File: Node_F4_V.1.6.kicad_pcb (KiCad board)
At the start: 2 copper layers, 56 x 100 mm, 171 parts, among them IC2 MP1584EN, J1 Conn_Jack-DC, J2 Conn_02x12_Odd_Even, J3 Micro_SD_Card, J4 RF_IPEX_U.FL-R-SMT, J5 Conn_01x06, J6 Conn_01x06, J7 RS485, J8 LoRa_Anten, Q2 MMBT3904L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

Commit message: DI track
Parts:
- removed C50: 5.6pF, Anh_Footprints:C_0603
- removed C54: 100nF, Anh_Footprints:C_0603
- removed C58: 10uF, Anh_Footprints:C_0603
- removed C59: 1uF, Anh_Footprints:C_0603
- removed R46: TBD, Anh_Footprints:R_0603
- removed Z2: D_Zener, IVS_FOOTPRINTS:D_MiniMELF
- added C39: NC, Anh_Footprints:C_0603, F.Cu at (124.5, 54.8)
- added C41: 100nF, Anh_Footprints:C_0603, F.Cu at (138.3, 85.4)
- added R23: 10K, Anh_Footprints:R_0603, F.Cu at (155.7, 78.2)
- C51: value 2.4pF -> NC
- C71, C72: value 6.8pF -> NC
- D9, Q2, Q3: footprint IVS_FOOTPRINTS:SOT23-3 -> Anh_Footprints:SOT23-3
- J2: value Conn_02x12_Odd_Even -> IDC_LCD_KEYPAD
- J4: footprint Connector_Coaxial:U.FL_Hirose_U.FL-R-SMT-1_Vertical -> Anh_Footprints:IPEX_Antena_Connector
- J5: value Conn_01x06 -> SWD
- J6: value Conn_01x06 -> WiFi_Prog
- L4: value 2.7nH -> 2.2nH
- U4: footprint Package_SO:SOIC-8_5.23x5.23mm_P1.27mm -> Anh_Footprints:SOIC-8_5.23x5.23
- U5: footprint IVS_FOOTPRINTS:SOIC-16W_7.5x10.3mm_P1.27mm -> Package_SO:SOIC-16W_7.5x10.3mm_P1.27mm
- Y1, Y2: footprint IVS_FOOTPRINTS:Crystal_SMD_5032-4Pin_5.0x3.2mm -> Anh_Footprints:Crystal_3225_4P_1-4
- moved Q2 85.4 mm to (155.2, 80.6)
- moved C9 79.5 mm to (140.2, 116.2), turned to 90 degrees
- moved C51 78.5 mm to (124.5, 50.5), turned to 180 degrees
- moved C55 76.9 mm to (120.2, 51.8), turned to 180 degrees
- moved C52 76.6 mm to (122.3, 54.1), turned to -90 degrees
- moved L5 76.6 mm to (121.0, 54.1), turned to -90 degrees
- moved C38 76.3 mm to (128.9, 53.8), turned to 0 degrees
- moved L4 75.6 mm to (125.2, 52.6)
- moved BZ1 75.4 mm to (146.2, 86.2), turned to 90 degrees
- moved C10 74.8 mm to (126.8, 54.5), turned to 90 degrees
- moved C40 74.4 mm to (128.9, 55.3), turned to 180 degrees
- moved R42 73.9 mm to (156.5, 84.2), turned to -90 degrees
- moved C56 73.8 mm to (119.5, 54.1)
- moved D11 73.8 mm to (151.4, 106.1), turned to 180 degrees
- moved C53 73.3 mm to (119.6, 60.8)
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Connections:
- C45 pad 2: Net-(C45-Pad2) -> Net-(U6-XTAL_P)
- J7 pad 1: GND -> /A+
- J7 pad 2: /A+ -> /B-
- J7 pad 3: /B- -> GND
- L4 pad 1: Net-(U6-LNA_IN) -> Net-(J4-In)
- L4 pad 2: GND -> Net-(U6-LNA_IN)
- U3 pad 1: /BUZZER -> unconnected-(U3-PE2-Pad1)
- U3 pad 7: unconnected-(U3-PC13-Pad7) -> Net-(D1-A)
- U3 pad 71: unconnected-(U3-PA12-Pad71) -> /BUZZER
- U3 pad 72: unconnected-(U3-PA13-Pad72) -> /SWDIO
- U3 pad 76: unconnected-(U3-PA14-Pad76) -> /SWCLK
- U3 pad 9: Net-(D1-A) -> unconnected-(U3-PC15-Pad9)
- Y2 pad 1: Net-(C45-Pad2) -> Net-(U6-XTAL_P)
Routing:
- net +3.3V: track 107.0 -> 404.6 mm, vias 0 -> 28
- net GND: track 7.19 -> 59.0 mm, vias 0 -> 6
- net /SWDIO: track 0.00 -> 48.6 mm, vias 0 -> 1
- net VCC: track 0.00 -> 46.3 mm, vias 0 -> 2
- net /ESP_RX: track 1.55 -> 45.2 mm
- net /I2C_SCL: track 0.00 -> 41.0 mm, vias 0 -> 2
- net /SWCLK: track 0.00 -> 40.0 mm, vias 0 -> 1
- net /I2C_SDA: track 0.00 -> 38.4 mm, vias 0 -> 2
- net /UART_TX_LOG: track 0.00 -> 34.7 mm, vias 0 -> 1
- net /UART_RX_LOG: track 0.00 -> 33.9 mm, vias 0 -> 1
- net /ESP_TX: track 10.8 -> 43.3 mm
- net /LORA NSS: track 0.00 -> 30.7 mm, vias 0 -> 2
- net /SPI_MOSI: track 0.00 -> 28.6 mm, vias 0 -> 2
- net /RS485_RO: track 1.48 -> 28.5 mm, vias 0 -> 2
- net /SPI_MISO: track 0.00 -> 26.6 mm, vias 0 -> 2
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- added copper zone on B.Cu, net GND
- added copper zone on F.Cu, net GND

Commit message: 50%
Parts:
- removed C41: 100nF, Anh_Footprints:C_0603
- removed D1: LED_Blink, Anh_Footprints:LED_0603
- removed R13: 470, Anh_Footprints:R_0603
- removed R36, R37, R38, R39, R40: 10k, Anh_Footprints:R_0603
- added C50: 1u, Anh_Footprints:C_0603, F.Cu at (100.1, 118.2)
- added C54: 100n, Anh_Footprints:C_0603, F.Cu at (98.4, 118.2)
- added D12: LED, Anh_Footprints:LED_0603, F.Cu at (116.4, 75.2)
- added D13: LED, Anh_Footprints:LED_0603, F.Cu at (120.1, 75.2)
- added D2: LED, Anh_Footprints:LED_0603, F.Cu at (108.8, 75.3)
- added D6: LED, Anh_Footprints:LED_0603, F.Cu at (112.6, 75.2)
- added Q1: P_Mosfet, Anh_Footprints:SOT23-3, F.Cu at (82.5, 101.8)
- added R24: 1M, Anh_Footprints:R_0603, F.Cu at (85.2, 101.6)
- added R25: 220, Anh_Footprints:R_0603, F.Cu at (108.8, 76.7)
- added R26: 220, Anh_Footprints:R_0603, F.Cu at (112.6, 76.6)
- added R27: 220, Anh_Footprints:R_0603, F.Cu at (116.4, 76.6)
- added R28: 220, Anh_Footprints:R_0603, F.Cu at (120.1, 76.6)
- added U7: W25Q128JVS, IVS_FOOTPRINTS:SOIC-8_5.23x5.23mm_P1.27mm, F.Cu at (92.8, 120.1)
- C13: footprint Anh_Footprints:C_0603 -> Anh_Footprints:C_1210
- J2: value IDC_LCD_KEYPAD -> Conn_01x10; footprint Connector_IDC:IDC-Header_2x12_P2.54mm_Vertical -> IVS_FOOTPRINTS:XH 2.54 10Pin Female
- J3: value Micro_SD_Card -> Conn_01x16_Female; footprint Anh_Footprints:MicroSD_Socket_9P -> Connector_PinSocket_2.54mm:PinSocket_1x16_P2.54mm_Vertical
- moved H1 124.2 mm to (75.7, 122.4), turned to 180 degrees
- moved H4 115.3 mm to (75.7, 69.3), turned to 180 degrees
- moved H2 93.5 mm to (167.7, 122.4), turned to 180 degrees
- moved C26 88.5 mm to (86.3, 114.7), turned to 180 degrees
- moved C6 87.6 mm to (86.3, 113.0), turned to 180 degrees
- moved C25 83.2 mm to (86.9, 101.6), turned to 90 degrees
- moved H3 81.2 mm to (167.7, 69.3), turned to 180 degrees
- moved L1 78.5 mm to (88.4, 95.3), turned to 0 degrees
- moved C19 78.1 mm to (88.4, 97.0), turned to 0 degrees
- moved C12 77.7 mm to (88.4, 98.7), turned to 180 degrees
- moved C28 73.8 mm to (92.3, 97.1), turned to 90 degrees
- moved C24 69.4 mm to (94.0, 97.2), turned to 90 degrees
- moved C8 68.4 mm to (94.9, 94.7), turned to 180 degrees
- moved Y1 66.6 mm to (96.5, 91.9), turned to 180 degrees
- moved R3 64.9 mm to (96.4, 97.0), turned to 0 degrees
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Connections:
- J2 pad 1: GND -> unconnected-(J2-Pin_1-Pad1)
- J2 pad 2: unconnected-(J2-Pin_2-Pad2) -> /C1
- J2 pad 3: +3.3V -> /C2
- J2 pad 4: unconnected-(J2-Pin_4-Pad4) -> /C3
- J2 pad 5: /TFT_CS -> /C4
- J2 pad 6: unconnected-(J2-Pin_6-Pad6) -> /H1
- J2 pad 7: /TFT_RS -> /H2
- J2 pad 8: unconnected-(J2-Pin_8-Pad8) -> /H3
- J2 pad 9: /TFT_WR -> /H4
- J3 pad 1: /SD_D2 -> GND
- J3 pad 2: /SD_D3 -> +3.3V
- J3 pad 3: /SD_CMD -> /TFT_CS
- J3 pad 4: +3.3V -> /TFT_RS
- J3 pad 5: /SD_CLK -> /TFT_WR
- J3 pad 6: GND -> /TFT_RD
- J3 pad 7: /SD_D0 -> /TFT_RST
- J3 pad 8: /SD_D1 -> Net-(J3-Pin_8)
- J3 pad 9: GND -> /TFT_DB0
- U3 pad 1: unconnected-(U3-PE2-Pad1) -> /TFT_RST
- U3 pad 2: unconnected-(U3-PE3-Pad2) -> /TFT_RD
- U3 pad 3: unconnected-(U3-PE4-Pad3) -> /TFT_WR
- U3 pad 39: unconnected-(U3-PE8-Pad39) -> /TFT_DB0
- U3 pad 4: unconnected-(U3-PE5-Pad4) -> /TFT_RS
- U3 pad 40: unconnected-(U3-PE9-Pad40) -> /TFT_DB1
- U3 pad 41: unconnected-(U3-PE10-Pad41) -> /TFT_DB2
- U3 pad 42: unconnected-(U3-PE11-Pad42) -> /TFT_DB3
- U3 pad 43: unconnected-(U3-PE12-Pad43) -> /TFT_DB4
- U3 pad 44: unconnected-(U3-PE13-Pad44) -> /TFT_DB5
- U3 pad 45: unconnected-(U3-PE14-Pad45) -> /TFT_DB6
- U3 pad 46: unconnected-(U3-PE15-Pad46) -> /TFT_DB7
- U3 pad 48: unconnected-(U3-PB11-Pad48) -> /BUZZER
- U3 pad 5: unconnected-(U3-PE6-Pad5) -> /TFT_CS
- U3 pad 51: unconnected-(U3-PB12-Pad51) -> /W25Q_CS
- U3 pad 65: /SD_D0 -> unconnected-(U3-PC8-Pad65)
- U3 pad 66: /SD_D1 -> unconnected-(U3-PC9-Pad66)
- U3 pad 7: Net-(D1-A) -> unconnected-(U3-PC13-Pad7)
- U3 pad 71: /BUZZER -> unconnected-(U3-PA12-Pad71)
- U3 pad 77: unconnected-(U3-PA15-Pad77) -> /H1
- U3 pad 78: /SD_D2 -> /H2
- U3 pad 79: /SD_D3 -> /H3
- U3 pad 80: /SD_CLK -> /H4
- U3 pad 81: unconnected-(U3-PD0-Pad81) -> /C4
- U3 pad 82: unconnected-(U3-PD1-Pad82) -> /C3
- U3 pad 83: /SD_CMD -> /C2
- U3 pad 84: unconnected-(U3-PD3-Pad84) -> /C1
- U3 pad 98: unconnected-(U3-PE1-Pad98) -> /TFT_LED
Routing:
- net /BUZZER: track 2.09 -> 97.8 mm, vias 0 -> 2
- net +3.3V: track 404.6 -> 497.1 mm, vias 28 -> 13
- net /H4: track 0.00 -> 80.4 mm, vias 0 -> 1
- net /C1: track 0.00 -> 78.4 mm, vias 0 -> 1
- net /H3: track 0.00 -> 76.7 mm, vias 0 -> 1
- net /C2: track 0.00 -> 75.7 mm, vias 0 -> 1
- net /C3: track 0.00 -> 72.8 mm, vias 0 -> 1
- net /H2: track 0.00 -> 70.9 mm, vias 0 -> 1
- net /C4: track 0.00 -> 70.8 mm, vias 0 -> 1
- net /SPI_MOSI: track 28.6 -> 96.7 mm
- net /H1: track 0.00 -> 67.5 mm, vias 0 -> 1
- net /SPI_SCK: track 24.3 -> 89.4 mm, vias 2 -> 3
- net /SPI_MISO: track 26.6 -> 91.2 mm
- net /LORA_RST: track 20.3 -> 80.0 mm, vias 0 -> 2
- net GND: track 59.0 -> 0.00 mm, vias 6 -> 66
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- added copper zone on F.Cu, net Net-(D8-K)
- added copper zone on F.Cu, net Net-(F1-Pad1)
- added copper zone on F.Cu, net Net-(JP2-A)
- added copper zone on F.Cu, net VCC
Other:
- board size 56 x 100 mm -> 97.5 x 59 mm
- board text added: "3v3"
- board text added: "BOOT"
- board text added: "CLK"
- board text added: "DIO"
- board text added: "ESP NAP CODE"
- board text added: "GND"
- board text added: "RST"
- board text added: "RX"
- board text added: "STM NAP CODE"
- board text added: "TX"

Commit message: Xep linh kien
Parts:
- moved BT1 42.0 mm to (87.8, 97.6), turned to 90 degrees
- moved SW1 31.9 mm to (91.6, 118.3), turned to -90 degrees
- moved J6 31.2 mm to (99.2, 118.2)
- moved SW3 31.1 mm to (86.8, 118.3), turned to 90 degrees
- moved C12 29.0 mm to (114.4, 85.8)
- moved C19 28.9 mm to (114.4, 84.4)
- moved L1 28.8 mm to (114.4, 83.0)
- moved U7 28.6 mm to (118.9, 108.4), turned to 180 degrees
- moved C42 27.1 mm to (89.0, 113.8)
- moved C3 26.8 mm to (86.2, 113.8)
- moved SW2 26.6 mm to (82.5, 118.3), turned to -90 degrees
- moved R11 26.6 mm to (87.6, 113.8)
- moved R24 25.9 mm to (108.2, 89.8)
- moved C8 25.8 mm to (117.8, 82.8)
- moved C24 25.8 mm to (116.8, 85.1)
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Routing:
- net +3.3V: track 497.1 -> 14.7 mm, vias 13 -> 0
- net /BUZZER: track 97.8 -> 0.00 mm, vias 2 -> 0
- net /SPI_MOSI: track 96.7 -> 0.00 mm, vias 2 -> 0
- net /SPI_MISO: track 91.2 -> 0.00 mm, vias 2 -> 0
- net /SPI_SCK: track 89.4 -> 0.00 mm, vias 3 -> 0
- net /LORA NSS: track 86.8 -> 0.00 mm, vias 2 -> 0
- net /H4: track 80.4 -> 0.00 mm, vias 1 -> 0
- net /LORA_RST: track 80.0 -> 0.00 mm, vias 2 -> 0
- net /LORA_DIO1: track 78.9 -> 0.00 mm, vias 2 -> 0
- net /C1: track 78.4 -> 0.00 mm, vias 1 -> 0
- net /LORA_DIO0: track 78.4 -> 0.00 mm, vias 2 -> 0
- net /H3: track 76.7 -> 0.00 mm, vias 1 -> 0
- net /C2: track 75.7 -> 0.00 mm, vias 1 -> 0
- net /C3: track 72.8 -> 0.00 mm, vias 1 -> 0
- net /H2: track 70.9 -> 0.00 mm, vias 1 -> 0
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- removed copper zone on B.Cu, net GND
- removed copper zone on F.Cu, net GND
- removed copper zone on F.Cu, net Net-(D8-K)
- removed copper zone on F.Cu, net Net-(F1-Pad1)
- removed copper zone on F.Cu, net Net-(JP2-A)
- removed copper zone on F.Cu, net VCC
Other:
- board text removed: "3v3"
- board text removed: "BOOT"
- board text removed: "CLK"
- board text removed: "DIO"
- board text removed: "ESP NAP CODE"
- board text removed: "GND"
- board text removed: "RST"
- board text removed: "RX"
- board text removed: "STM NAP CODE"
- board text removed: "TX"

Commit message: Layout gan xong
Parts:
- added R13: 1k, Anh_Footprints:R_0603, F.Cu at (113.6, 71.7)
- added R29: 1k, Anh_Footprints:R_0603, F.Cu at (110.8, 71.7)
- added R30: 1k, Anh_Footprints:R_0603, F.Cu at (108.0, 71.7)
- added R31: 1k, Anh_Footprints:R_0603, F.Cu at (105.2, 71.7)
- moved R28 30.6 mm to (103.8, 71.7), turned to 90 degrees
- moved D13 29.6 mm to (104.4, 73.9)
- moved R27 24.5 mm to (106.6, 71.7), turned to 90 degrees
- moved D12 23.3 mm to (107.2, 73.9)
- moved R26 18.7 mm to (109.4, 71.7), turned to 90 degrees
- moved D6 17.3 mm to (110.0, 73.9)
- moved R25 13.0 mm to (112.2, 71.7), turned to 90 degrees
- moved D2 11.4 mm to (112.8, 73.9)
- moved C57 11.2 mm to (96.7, 82.1)
- moved D10 8.40 mm to (132.6, 101.4), turned to 180 degrees
- moved R50 7.54 mm to (132.6, 100.0)
- moved R53 7.00 mm to (132.6, 97.2)
- moved R54 5.05 mm to (132.6, 98.6)
- moved J2 4.21 mm to (120.4, 70.7)
- moved D11 4.20 mm to (132.6, 95.8)
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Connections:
- J5 pad 1: /SWCLK -> /UART_RX_LOG
- J5 pad 2: /SWDIO -> /UART_TX_LOG
- J5 pad 3: GND -> +3.3V
- J5 pad 4: +3.3V -> GND
- J5 pad 5: /UART_TX_LOG -> /SWDIO
- J5 pad 6: /UART_RX_LOG -> /SWCLK
- J6 pad 1: /ESP_TX_LOAD -> /ESP_BOOT
- J6 pad 2: /ESP_RX_LOAD -> /ESP_RST
- J6 pad 3: GND -> +3.3V
- J6 pad 4: +3.3V -> GND
- J6 pad 5: /ESP_RST -> /ESP_RX_LOAD
- J6 pad 6: /ESP_BOOT -> /ESP_TX_LOAD
- U1 pad 16: /SPI_SCK -> /SPI3_SCK
- U1 pad 17: /SPI_MISO -> /SPI3_MISO
- U1 pad 18: /SPI_MOSI -> /SPI3_MOSI
- U1 pad 8: /LORA_DIO0 -> /LORA_INT
- U1 pad 9: /LORA_DIO1 -> unconnected-(U1-DIO1-Pad9)
- U3 pad 23: /RS485_DI -> unconnected-(U3-PA0-Pad23)
- U3 pad 24: /RS485_RO -> unconnected-(U3-PA1-Pad24)
- U3 pad 25: /RS485_DERE -> /ESP_RX
- U3 pad 26: unconnected-(U3-PA3-Pad26) -> /ESP_TX
- U3 pad 31: unconnected-(U3-PA6-Pad31) -> /C1
- U3 pad 32: unconnected-(U3-PA7-Pad32) -> /C2
- U3 pad 33: unconnected-(U3-PC4-Pad33) -> /C3
- U3 pad 34: unconnected-(U3-PC5-Pad34) -> /C4
- U3 pad 35: unconnected-(U3-PB0-Pad35) -> /H1
- U3 pad 36: unconnected-(U3-PB1-Pad36) -> /H2
- U3 pad 37: unconnected-(U3-PB2-Pad37) -> /H3
- U3 pad 38: unconnected-(U3-PE7-Pad38) -> /H4
- U3 pad 47: unconnected-(U3-PB10-Pad47) -> /I2C_SCL
- U3 pad 48: /BUZZER -> /I2C_SDA
- U3 pad 51: /W25Q_CS -> unconnected-(U3-PB12-Pad51)
- U3 pad 52: /SPI_SCK -> /SPI2_SCK
- U3 pad 53: /SPI_MISO -> /SPI2_MISO
- U3 pad 54: /SPI_MOSI -> /SPI2_MOSI
- U3 pad 55: /LORA NSS -> /W25Q_CS
- U3 pad 60: /LORA_DIO1 -> unconnected-(U3-PD13-Pad60)
- U3 pad 61: /LORA_DIO0 -> unconnected-(U3-PD14-Pad61)
- U3 pad 62: /LORA_RST -> unconnected-(U3-PD15-Pad62)
- U3 pad 68: /ESP_RX -> /UART_TX_LOG
- U3 pad 69: /ESP_TX -> /UART_RX_LOG
- U3 pad 77: /H1 -> unconnected-(U3-PA15-Pad77)
- U3 pad 78: /H2 -> unconnected-(U3-PC10-Pad78)
- U3 pad 79: /H3 -> unconnected-(U3-PC11-Pad79)
- U3 pad 80: /H4 -> /RS485_DI
- U3 pad 81: /C4 -> unconnected-(U3-PD0-Pad81)
- U3 pad 82: /C3 -> /RS485_DERE
- U3 pad 83: /C2 -> /RS485_RO
- U3 pad 84: /C1 -> /LORA_INT
- U3 pad 86: /UART_TX_LOG -> /LORA_RST
- U3 pad 87: /UART_RX_LOG -> unconnected-(U3-PD6-Pad87)
- U3 pad 89: unconnected-(U3-PB3-Pad89) -> /SPI3_SCK
- U3 pad 90: unconnected-(U3-PB4-Pad90) -> /SPI3_MISO
- U3 pad 91: unconnected-(U3-PB5-Pad91) -> /SPI3_MOSI
- U3 pad 92: /I2C_SCL -> /LORA NSS
- U3 pad 93: /I2C_SDA -> unconnected-(U3-PB7-Pad93)
- U7 pad 2: /SPI_MISO -> /SPI2_MISO
- U7 pad 5: /SPI_MOSI -> /SPI2_MOSI
- U7 pad 6: /SPI_SCK -> /SPI2_SCK
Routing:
- net +3.3V: track 14.7 -> 499.1 mm, vias 0 -> 26
- net /ESP_BOOT: track 0.00 -> 76.9 mm, vias 0 -> 4
- net /ESP_RST: track 0.00 -> 69.9 mm, vias 0 -> 3
- net /C4: track 0.00 -> 67.2 mm, vias 0 -> 1
- net Net-(U3-NRST): track 0.00 -> 61.8 mm, vias 0 -> 4
- net /C3: track 0.00 -> 57.7 mm, vias 0 -> 1
- net /ESP_TX_LOAD: track 0.00 -> 53.3 mm, vias 0 -> 3
- net /TFT_RST: track 0.00 -> 52.6 mm, vias 0 -> 1
- net /TFT_DB3: track 0.00 -> 52.1 mm, vias 0 -> 1
- net /C2: track 0.00 -> 51.5 mm, vias 0 -> 1
- net /TFT_RD: track 0.00 -> 51.1 mm, vias 0 -> 1
- net /TFT_DB0: track 0.00 -> 51.1 mm, vias 0 -> 1
- net /TFT_DB1: track 0.00 -> 50.9 mm, vias 0 -> 1
- net /TFT_WR: track 0.00 -> 50.8 mm, vias 0 -> 1
- net /TFT_RS: track 0.00 -> 50.8 mm, vias 0 -> 1
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- added copper zone on B.Cu, net GND
- added copper zone on F.Cu, net GND
- added copper zone on F.Cu, net Net-(D8-K)
- added copper zone on F.Cu, net Net-(F1-Pad1)
- added copper zone on F.Cu, net Net-(JP2-A)
- added copper zone on F.Cu, net VCC

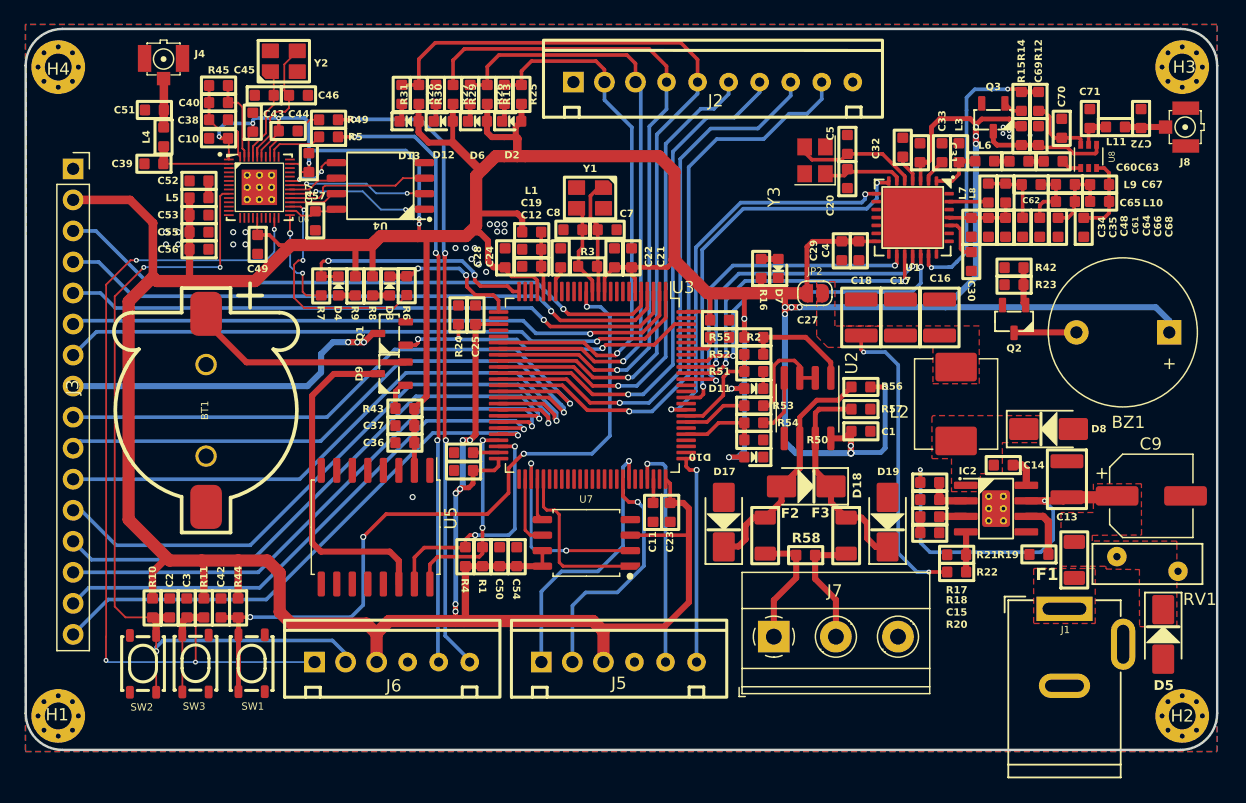
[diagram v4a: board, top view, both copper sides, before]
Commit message: Via not foundand connect  GND
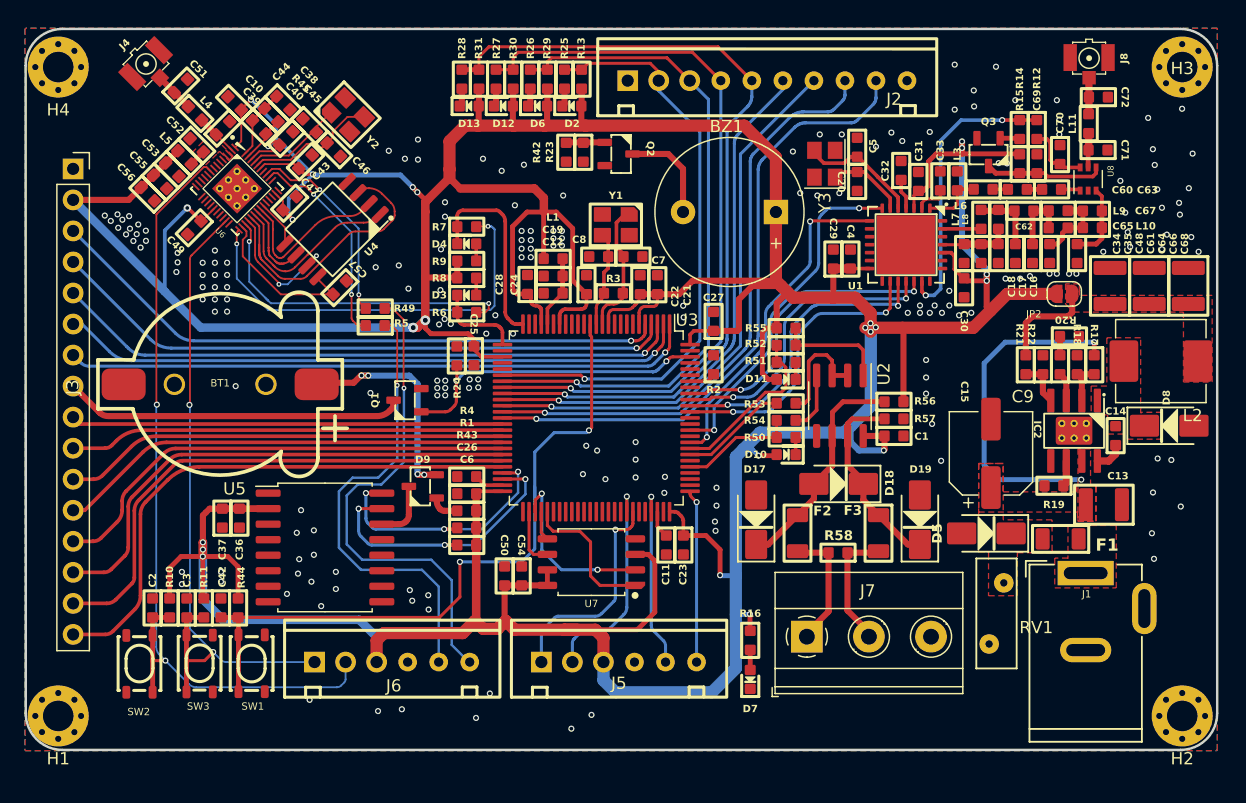
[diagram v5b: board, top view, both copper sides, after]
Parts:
- H1, H2, H3, H4: footprint MountingHole:MountingHole_2.2mm_M2_Pad_Via -> MountingHole:MountingHole_2.5mm_Pad_Via
- moved R42 37.8 mm to (117.2, 76.5), turned to -90 degrees
- moved R23 36.9 mm to (118.7, 76.5), turned to -90 degrees
- moved Q2 35.1 mm to (121.5, 76.6), turned to -90 degrees
- moved D7 33.7 mm to (132.3, 119.6)
- moved BZ1 33.7 mm to (134.4, 81.3)
- moved R16 30.4 mm to (132.3, 116.4), turned to -90 degrees
- moved C17 20.5 mm to (165.0, 87.4)
- moved C18 20.5 mm to (161.8, 87.4)
- moved C16 20.5 mm to (168.2, 87.4)
- moved JP2 20.4 mm to (158.0, 88.0)
- moved R20 19.7 mm to (158.4, 91.5)
- moved R22 17.9 mm to (154.9, 93.8), turned to 90 degrees
- moved L2 17.1 mm to (165.9, 93.5), turned to 0 degrees
- moved R21 17.1 mm to (156.3, 93.8), turned to 90 degrees
- moved C37 16.7 mm to (89.1, 106.4), turned to 90 degrees
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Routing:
- net Net-(U6-GPIO16): track 8.63 -> 34.9 mm
- net Net-(U5-VBAT): track 27.8 -> 4.96 mm
- net /ESP_BOOT: track 76.9 -> 55.9 mm, vias 4 -> 2
- net Net-(JP2-A): track 24.7 -> 8.32 mm, vias 2 -> 0
- net /TFT_DB0: track 51.1 -> 35.4 mm, vias 1 -> 0
- net /TFT_DB1: track 50.9 -> 35.6 mm, vias 1 -> 0
- net /TFT_DB3: track 52.1 -> 37.3 mm, vias 1 -> 0
- net /TFT_DB2: track 50.7 -> 36.4 mm, vias 1 -> 0
- net /ESP_TX_LOAD: track 53.3 -> 40.6 mm, vias 3 -> 1
- net Net-(U6-U0RXD): track 4.69 -> 17.4 mm, vias 0 -> 2
- net +3.3V: track 499.1 -> 511.1 mm, vias 26 -> 24
- net /SWP_SD3: track 12.0 -> 23.4 mm
- net Net-(U6-U0TXD): track 6.37 -> 16.6 mm, vias 0 -> 2
- net /ESP_RX_LOAD: track 50.2 -> 40.4 mm, vias 3 -> 1
- net /TFT_DB4: track 48.7 -> 39.1 mm, vias 1 -> 0
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- added copper zone on F.Cu, net Net-(C52-Pad2)

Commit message: Xong layout cho var
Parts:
- added G1: LOGO, Anh_Footprints:MU_Footprint, B.Cu at (121.1, 94.4)
- moved IC2 0.31 mm to (158.5, 99.2)
- moved Y1 0.19 mm to (121.3, 82.2)
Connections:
- U3 pad 24: unconnected-(U3-PA1-Pad24) -> /BUZZER
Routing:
- net /BUZZER: track 0.00 -> 18.7 mm, vias 0 -> 2
- net GND: track 0.12 -> 9.57 mm, vias 189 -> 181
- net +3.3V: track 511.1 -> 507.4 mm
- net /ESP_RX_LOAD: track 40.4 -> 37.5 mm
- net Net-(U1-VR_PA): track 5.84 -> 8.64 mm
- net Net-(C61-Pad1): track 5.52 -> 8.26 mm
- net Net-(U3-NRST): track 59.1 -> 58.2 mm
- net /ESP_BOOT: track 55.9 -> 55.3 mm
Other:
- board text added: "A+ B- GND RS485"
- board text added: "BOOT RST 3v3 GND RX TX ESP32"
- board text added: "DS3231 RTC"
- board text added: "ESP32 BOOT"
- board text added: "ESP32 RST"
- board text added: "FLASH W25Q"
- board text added: "KEYPAD"
- board text added: "LORA"
- board text added: "POWER 3v3"
- board text added: "RX TX 3v3 GND SWD SWC STM32"
- board text added: "SP3485"
- board text added: "STM32 RST"
- board text added: "STM32F407VET6"
- board text added: "TFT"
- board text added: "WIFI ESP32"
